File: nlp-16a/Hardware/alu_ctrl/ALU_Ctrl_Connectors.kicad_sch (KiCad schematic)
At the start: 85 parts, among them J1 Screw_Terminal_01x02, J10 Conn_02x08_Odd_Even, J2 Conn_02x20_Odd_Even, J3 Conn_02x10_Counter_Clockwise, J4 Conn_02x10_Counter_Clockwise, J5 Conn_02x10_Counter_Clockwise, J6 Conn_02x10_Counter_Clockwise, J7 Conn_02x10_Counter_Clockwise, J8 Conn_02x08_Odd_Even, J9 Conn_02x08_Odd_Even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

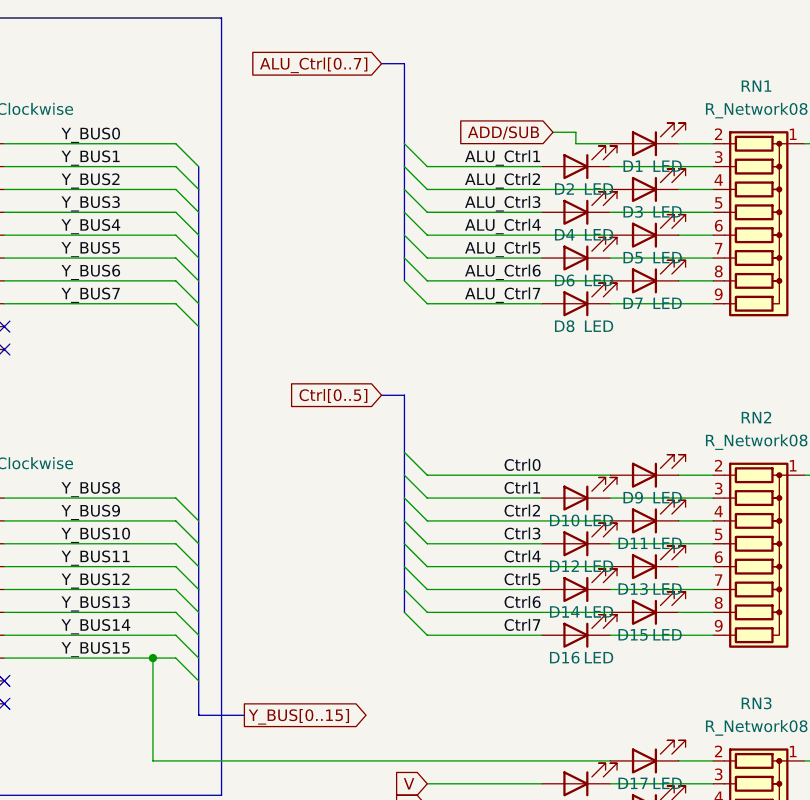
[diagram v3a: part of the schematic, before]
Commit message: Ctrlバス表示LED配線
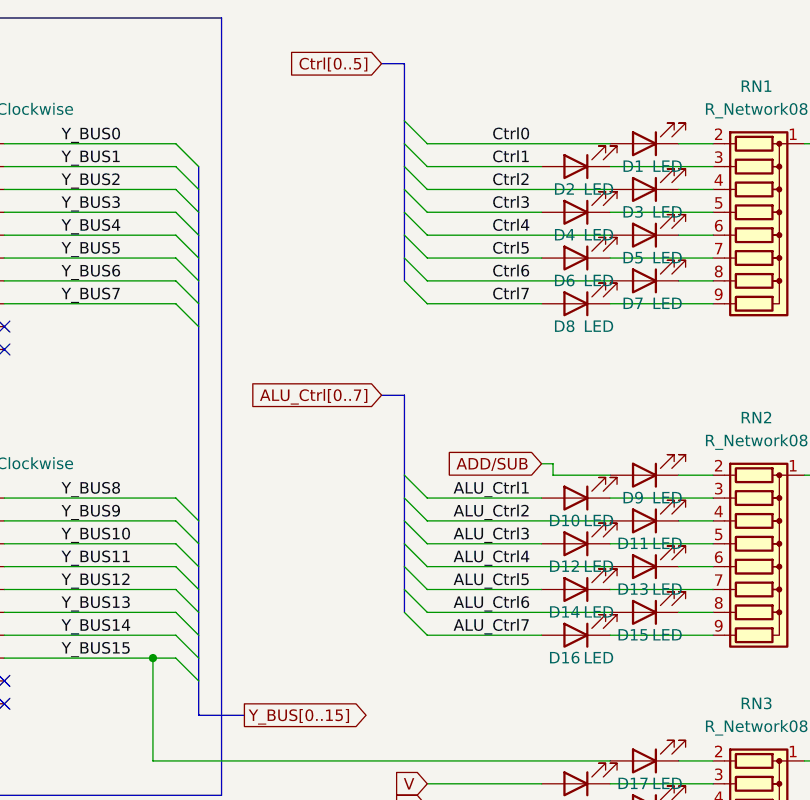
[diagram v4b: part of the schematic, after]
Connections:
- net ADD/SUB: now also D9.2 (A); no longer D1.2 (A)
- net ALU_Ctrl1: now also D10.2 (A); no longer D2.2 (A)
- net ALU_Ctrl2: now also D11.2 (A); no longer D3.2 (A)
- net ALU_Ctrl3: now also D12.2 (A); no longer D4.2 (A)
- net ALU_Ctrl4: now also D13.2 (A); no longer D5.2 (A)
- net ALU_Ctrl5: now also D14.2 (A); no longer D6.2 (A)
- net ALU_Ctrl6: now also D15.2 (A); no longer D7.2 (A)
- net ALU_Ctrl7: now also D16.2 (A); no longer D8.2 (A)
- net Ctrl0: now also D1.2 (A); no longer D9.2 (A)
- net Ctrl1: now also D2.2 (A); no longer D10.2 (A)
- net Ctrl2: now also D3.2 (A); no longer D11.2 (A)
- net Ctrl3: now also D4.2 (A); no longer D12.2 (A)
- net Ctrl4: now also D5.2 (A); no longer D13.2 (A)
- net Ctrl5: now also D6.2 (A); no longer D14.2 (A)
- net Ctrl6: now also D7.2 (A); no longer D15.2 (A)
- net Ctrl7: now also D8.2 (A); no longer D16.2 (A)
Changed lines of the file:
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@@
-    (stroke (width 0) (type default) (color 0 0 0 0))
-  )
-  (bus_entry (at 144.78 63.5) (size 2.54 2.54)
     (stroke (width 0) (type default) (color 0 0 0 0))
   )
@@
     (stroke (width 0) (type default) (color 0 0 0 0))
   )
+  (bus_entry (at 144.78 26.67) (size 2.54 2.54)
+    (stroke (width 0) (type default) (color 0 0 0 0))
+  )
   (bus_entry (at 144.78 31.75) (size 2.54 2.54)
     (stroke (width 0) (type default) (color 0 0 0 0))
@@
     (stroke (width 0) (type default) (color 0 0 0 0))
   )
+  (wire (pts (xy 160.02 64.77) (xy 161.29 64.77))
+    (stroke (width 0) (type default) (color 0 0 0 0))
+  )
   (wire (pts (xy 137.16 143.51) (xy 137.16 156.21))
     (stroke (width 0) (type default) (color 0 0 0 0))
@@
     (stroke (width 0) (type default) (color 0 0 0 0))
   )
+  (wire (pts (xy 161.29 64.77) (xy 161.29 66.04))
+    (stroke (width 0) (type default) (color 0 0 0 0))
+  )
   (wire (pts (xy 48.26 170.18) (xy 48.26 168.91))
     (stroke (width 0) (type default) (color 0 0 0 0))
@@
     (stroke (width 0) (type default) (color 0 0 0 0))
   )
+  (wire (pts (xy 161.29 66.04) (xy 167.64 66.04))
+    (stroke (width 0) (type default) (color 0 0 0 0))
+  )
   (bus (pts (xy 142.24 20.32) (xy 144.78 20.32))
     (stroke (width 0) (type default) (color 0 0 0 0))
@@
     (stroke (width 0) (type default) (color 0 0 0 0))
   )
-  (bus (pts (xy 144.78 20.32) (xy 144.78 29.21))
+  (bus (pts (xy 144.78 20.32) (xy 144.78 26.67))
     (stroke (width 0) (type default) (color 0 0 0 0))
   )
@@
     (stroke (width 0) (type default) (color 0 0 0 0))
   )
+  (bus (pts (xy 144.78 26.67) (xy 144.78 29.21))
+    (stroke (width 0) (type default) (color 0 0 0 0))
+  )
   (wire (pts (xy 161.29 154.94) (xy 173.99 154.94))
     (stroke (width 0) (type default) (color 0 0 0 0))
@@
     (stroke (width 0) (type default) (color 0 0 0 0))
   )
-  (bus (pts (xy 144.78 63.5) (xy 144.78 66.04))
+  (bus (pts (xy 144.78 57.15) (xy 144.78 66.04))
     (stroke (width 0) (type default) (color 0 0 0 0))
   )
@@
     (stroke (width 0) (type default) (color 0 0 0 0))
   )
+  (wire (pts (xy 147.32 29.21) (xy 167.64 29.21))
+    (stroke (width 0) (type default) (color 0 0 0 0))
+  )
   (wire (pts (xy 161.29 144.78) (xy 173.99 144.78))
     (stroke (width 0) (type default) (color 0 0 0 0))
@@
     (stroke (width 0) (type default) (color 0 0 0 0))
   )
-  (bus (pts (xy 144.78 57.15) (xy 144.78 63.5))
-    (stroke (width 0) (type default) (color 0 0 0 0))
-  )
   (wire (pts (xy 86.36 143.51) (xy 99.06 143.51))
     (stroke (width 0) (type default) (color 0 0 0 0))
@@
     (stroke (width 0) (type default) (color 0 0 0 0))
   )
-  (wire (pts (xy 163.83 27.94) (xy 163.83 29.21))
-    (stroke (width 0) (type default) (color 0 0 0 0))
-  )
   (wire (pts (xy 86.36 166.37) (xy 99.06 166.37))
     (stroke (width 0) (type default) (color 0 0 0 0))
@@
     (stroke (width 0) (type default) (color 0 0 0 0))
   )
-  (wire (pts (xy 161.29 27.94) (xy 163.83 27.94))
-    (stroke (width 0) (type default) (color 0 0 0 0))
-  )
   (wire (pts (xy 86.36 177.8) (xy 86.36 179.07))
     (stroke (width 0) (type default) (color 0 0 0 0))
@@
     (stroke (width 0) (type default) (color 0 0 0 0))
   )
-  (wire (pts (xy 147.32 66.04) (xy 167.64 66.04))
-    (stroke (width 0) (type default) (color 0 0 0 0))
-  )
   (wire (pts (xy 86.36 168.91) (xy 86.36 170.18))
     (stroke (width 0) (type default) (color 0 0 0 0))
@@
   )
   (wire (pts (xy 73.66 179.07) (xy 86.36 179.07))
-    (stroke (width 0) (type default) (color 0 0 0 0))
-  )
-  (wire (pts (xy 163.83 29.21) (xy 167.64 29.21))
     (stroke (width 0) (type default) (color 0 0 0 0))
   )
@@
     (effects (font (size 1.27 1.27)) (justify left bottom))
   )
-  (label "Ctrl5" (at 160.02 78.74 180)
+  (label "Ctrl5" (at 158.75 41.91 180)
     (effects (font (size 1.27 1.27)) (justify right bottom))
   )
@@
     (effects (font (size 1.27 1.27)) (justify left bottom))
   )
-  (label "ALU_Ctrl3" (at 160.02 36.83 180)
+  (label "ALU_Ctrl3" (at 158.75 73.66 180)
     (effects (font (size 1.27 1.27)) (justify right bottom))
   )
@@
     (effects (font (size 1.27 1.27)) (justify left bottom))
   )
-  (label "Ctrl2" (at 160.02 71.12 180)
+  (label "Ctrl2" (at 158.75 34.29 180)
     (effects (font (size 1.27 1.27)) (justify right bottom))
   )
@@
     (effects (font (size 1.27 1.27)) (justify left bottom))
   )
-  (label "ALU_Ctrl2" (at 160.02 34.29 180)
+  (label "ALU_Ctrl2" (at 158.75 71.12 180)
     (effects (font (size 1.27 1.27)) (justify right bottom))
   )
@@
     (effects (font (size 1.27 1.27)) (justify left bottom))
   )
-  (label "ALU_Ctrl5" (at 160.02 41.91 180)
+  (label "ALU_Ctrl5" (at 158.75 78.74 180)
     (effects (font (size 1.27 1.27)) (justify right bottom))
   )
-  (label "Ctrl0" (at 160.02 66.04 180)
+  (label "Ctrl0" (at 158.75 29.21 180)
     (effects (font (size 1.27 1.27)) (justify right bottom))
   )
@@
     (effects (font (size 1.27 1.27)) (justify left bottom))
   )
-  (label "Ctrl6" (at 160.02 81.28 180)
+  (label "Ctrl6" (at 158.75 44.45 180)
     (effects (font (size 1.27 1.27)) (justify right bottom))
   )
@@
     (effects (font (size 1.27 1.27)) (justify left bottom))
   )
-  (label "Ctrl4" (at 160.02 76.2 180)
+  (label "Ctrl4" (at 158.75 39.37 180)
     (effects (font (size 1.27 1.27)) (justify right bottom))
   )
@@
     (effects (font (size 1.27 1.27)) (justify left bottom))
   )
-  (label "ALU_Ctrl7" (at 160.02 46.99 180)
+  (label "ALU_Ctrl7" (at 158.75 83.82 180)
     (effects (font (size 1.27 1.27)) (justify right bottom))
   )
@@
     (effects (font (size 1.27 1.27)) (justify left bottom))
   )
-  (label "Ctrl7" (at 160.02 83.82 180)
+  (label "Ctrl7" (at 158.75 46.99 180)
     (effects (font (size 1.27 1.27)) (justify right bottom))
   )
@@
     (effects (font (size 1.27 1.27)) (justify left bottom))
   )
-  (label "Ctrl1" (at 160.02 68.58 180)
+  (label "Ctrl1" (at 158.75 31.75 180)
     (effects (font (size 1.27 1.27)) (justify right bottom))
   )
@@
     (effects (font (size 1.27 1.27)) (justify left bottom))
   )
-  (label "ALU_Ctrl6" (at 160.02 44.45 180)
+  (label "ALU_Ctrl6" (at 158.75 81.28 180)
     (effects (font (size 1.27 1.27)) (justify right bottom))
   )
-  (label "Ctrl3" (at 160.02 73.66 180)
+  (label "Ctrl3" (at 158.75 36.83 180)
     (effects (font (size 1.27 1.27)) (justify right bottom))
   )
-  (label "ALU_Ctrl1" (at 160.02 31.75 180)
+  (label "ALU_Ctrl1" (at 158.75 68.58 180)
     (effects (font (size 1.27 1.27)) (justify right bottom))
   )
@@
     (effects (font (size 1.27 1.27)) (justify left bottom))
   )
-  (label "ALU_Ctrl4" (at 160.02 39.37 180)
+  (label "ALU_Ctrl4" (at 158.75 76.2 180)
     (effects (font (size 1.27 1.27)) (justify right bottom))
   )
@@
     )
   )
-  (global_label "ADD{slash}SUB" (shape input) (at 161.29 27.94 180) (fields_autoplaced)
+  (global_label "ADD{slash}SUB" (shape input) (at 160.02 64.77 180) (fields_autoplaced)
     (effects (font (size 1.27 1.27)) (justify right))
-    (property "Intersheet References" "${INTERSHEET_REFS}" (id 0) (at 150.1079 28.0194 0)
+    (property "Intersheet References" "${INTERSHEET_REFS}" (id 0) (at 148.8379 64.8494 0)
       (effects (font (size 1.27 1.27)) (justify right) hide)
     )
@@
     )
   )
-  (global_label "Ctrl[0..5]" (shape input) (at 142.24 57.15 180) (fields_autoplaced)
+  (global_label "Ctrl[0..5]" (shape input) (at 142.24 20.32 180) (fields_autoplaced)
     (effects (font (size 1.27 1.27)) (justify right))
-    (property "Intersheet References" "${INTERSHEET_REFS}" (id 0) (at 131.0579 57.0706 0)
+    (property "Intersheet References" "${INTERSHEET_REFS}" (id 0) (at 131.0579 20.2406 0)
       (effects (font (size 1.27 1.27)) (justify right) hide)
     )
@@
     )
   )
-  (global_label "ALU_Ctrl[0..7]" (shape input) (at 142.24 20.32 180) (fields_autoplaced)
+  (global_label "ALU_Ctrl[0..7]" (shape input) (at 142.24 57.15 180) (fields_autoplaced)
     (effects (font (size 1.27 1.27)) (justify right))
-    (property "Intersheet References" "${INTERSHEET_REFS}" (id 0) (at 126.6431 20.2406 0)
+    (property "Intersheet References" "${INTERSHEET_REFS}" (id 0) (at 126.6431 57.0706 0)
       (effects (font (size 1.27 1.27)) (justify right) hide)
     )

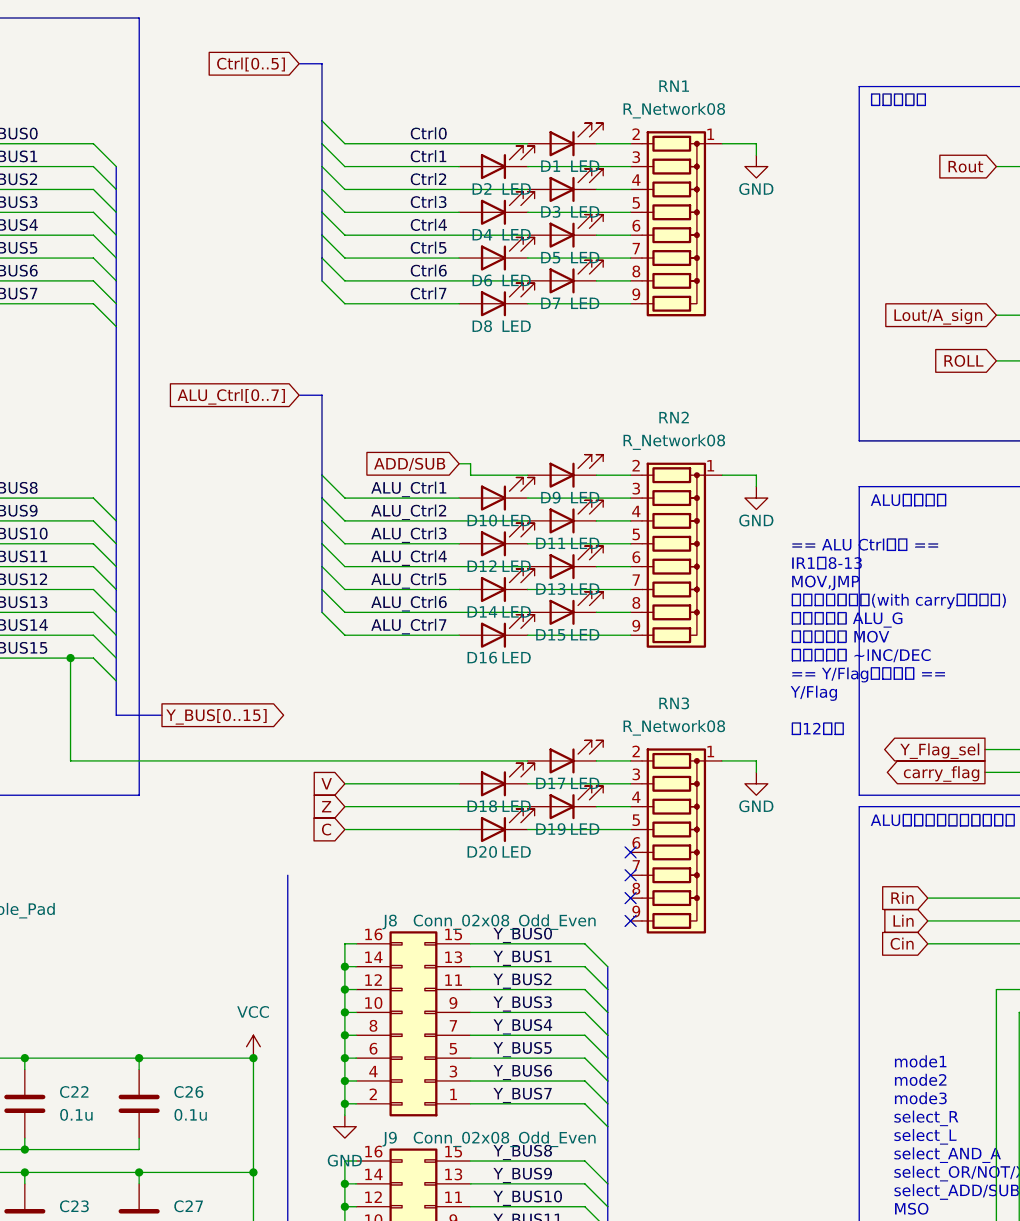
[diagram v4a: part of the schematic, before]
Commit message: だいたい終了残りは制御バスのデバッグポートのみ
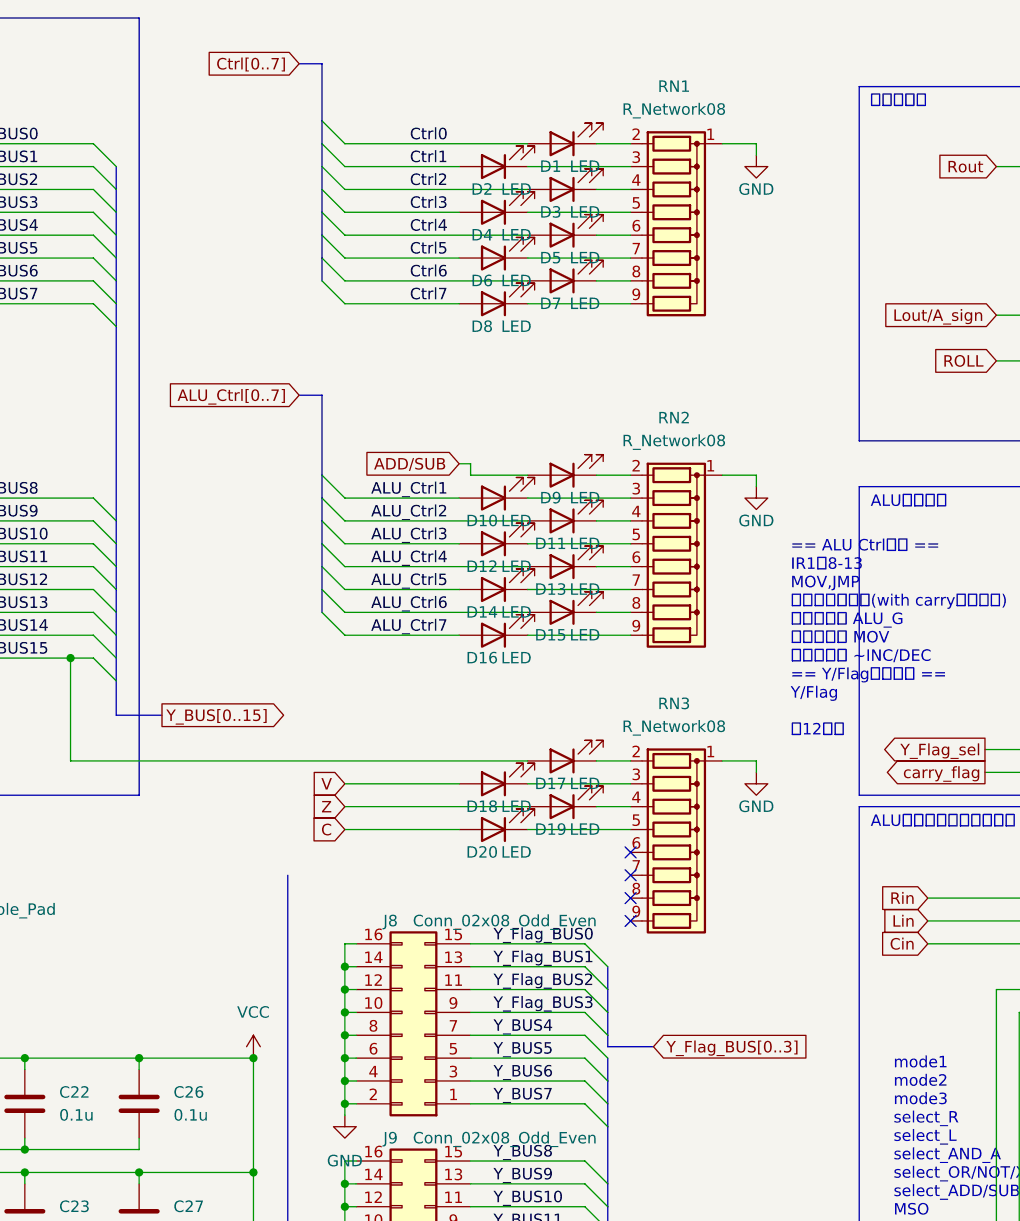
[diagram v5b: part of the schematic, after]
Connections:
- net Y_BUS0: no longer J8.15 (Pin_15)
- net Y_BUS1: no longer J8.13 (Pin_13)
- net Y_BUS2: no longer J8.11 (Pin_11)
- net Y_BUS3: no longer J8.9 (Pin_9)
- net Y_Flag_BUS0: now also J8.15 (Pin_15)
- net Y_Flag_BUS1: now also J8.13 (Pin_13)
- net Y_Flag_BUS2: now also J8.11 (Pin_11)
- net Y_Flag_BUS3: now also J8.9 (Pin_9)
